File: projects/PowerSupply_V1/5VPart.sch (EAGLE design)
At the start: 26 parts, among them IC1 LM2596T, IC2 LM2596T, X1 IN, X2 OUT

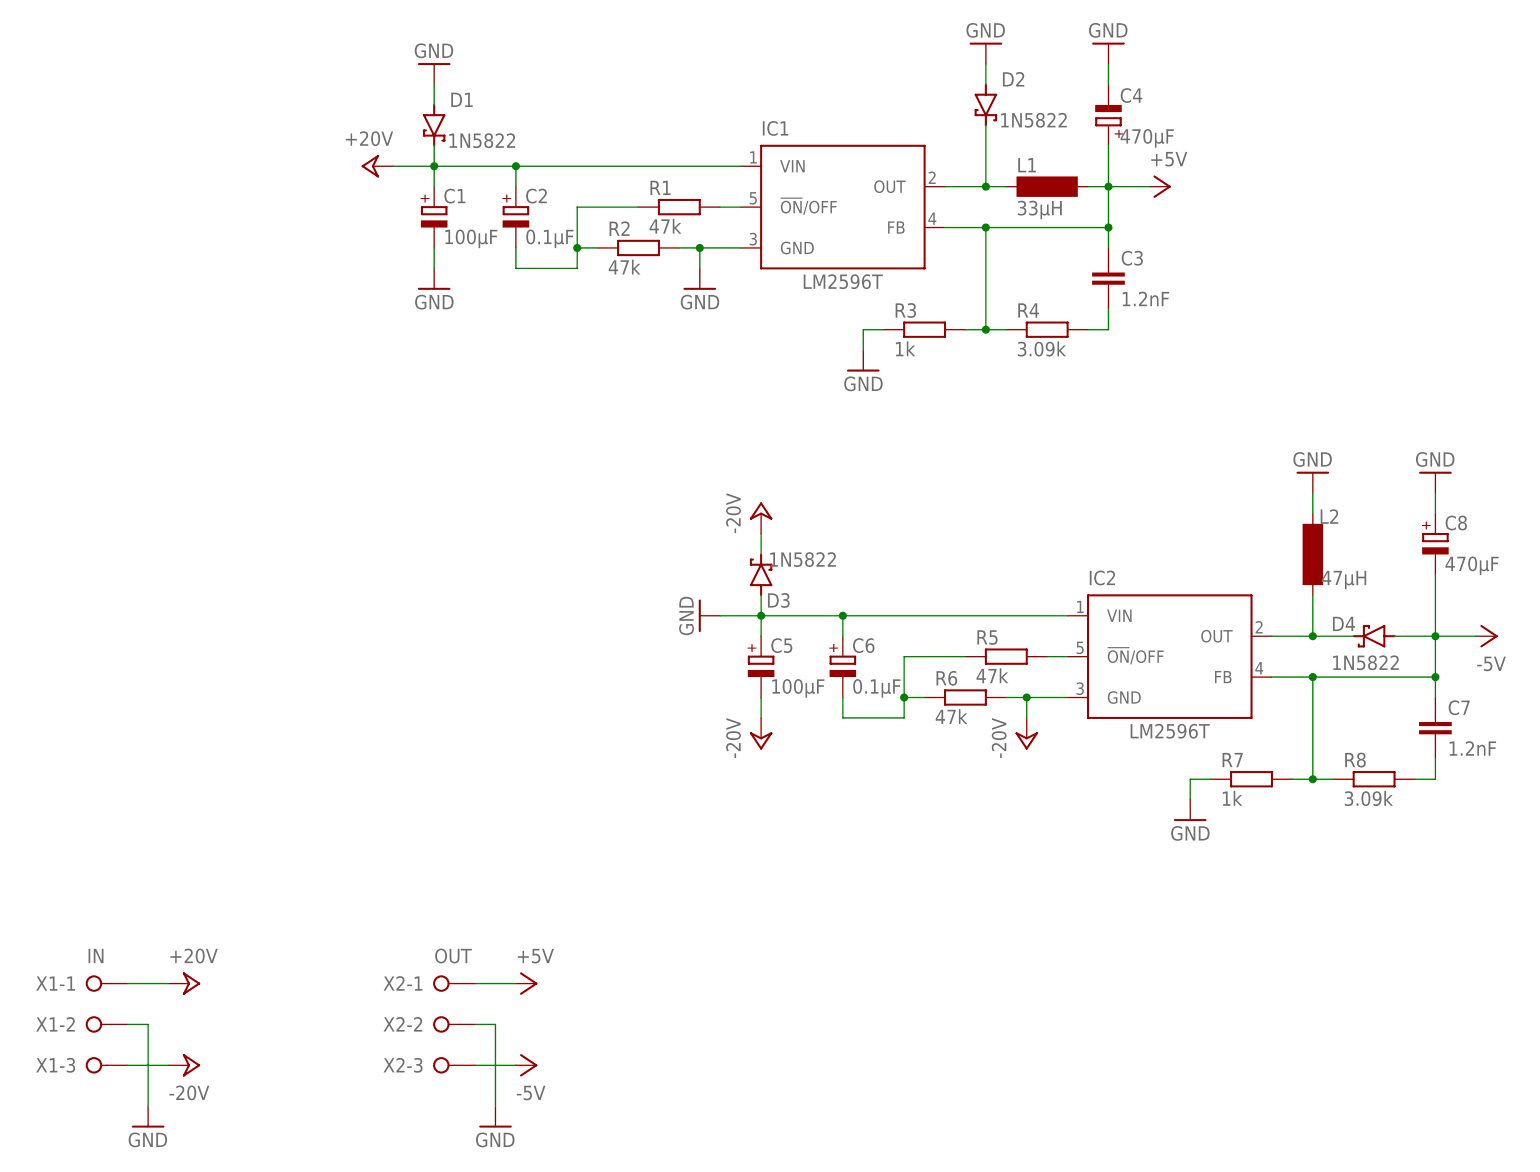
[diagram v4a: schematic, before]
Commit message: refactor(all): schematics and routing changed
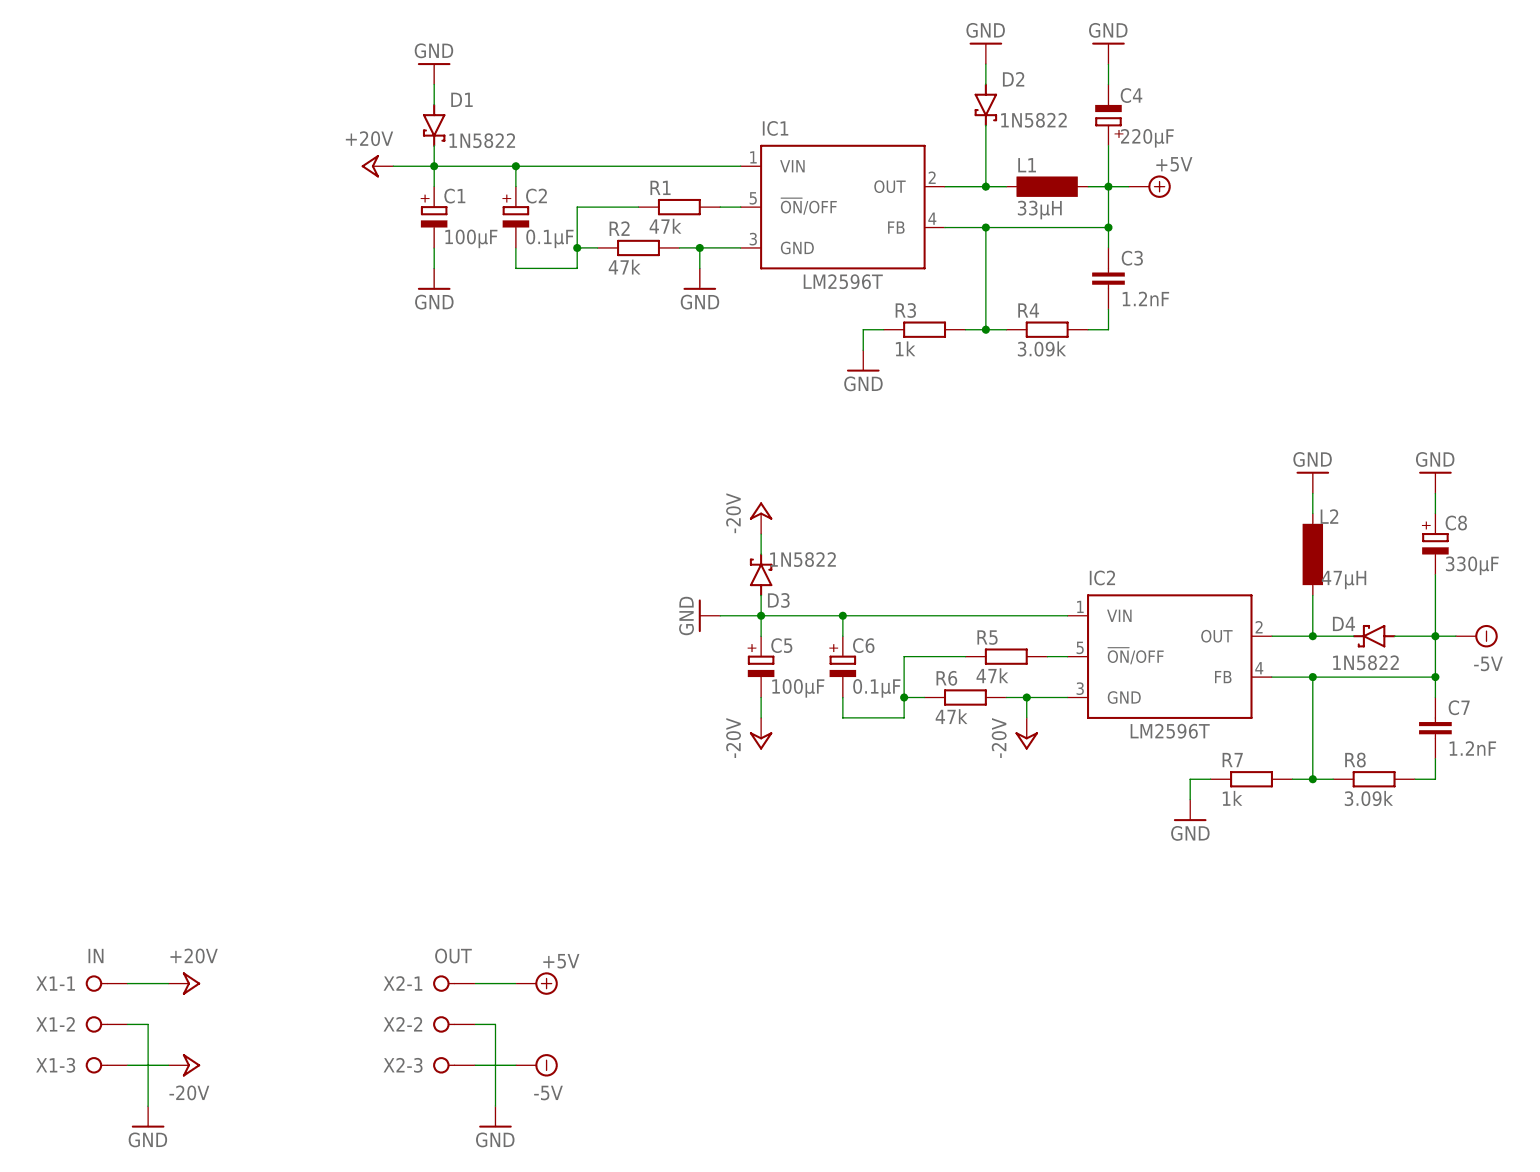
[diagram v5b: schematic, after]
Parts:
- C4: value 470µF -> 220µF
- C8: value 470µF -> 330µF
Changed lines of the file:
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@@
 <part name="GND5" library="supply1" library_urn="urn:adsk.eagle:library:371" deviceset="GND" device=""/>
 <part name="L1" library="inductor-neosid" library_urn="urn:adsk.eagle:library:241" deviceset="SD12" device="-680" package3d_urn="urn:adsk.eagle:package:14657/1" value="33µH"/>
-<part name="C4" library="rcl" library_urn="urn:adsk.eagle:library:334" deviceset="CPOL-EU" device="E3.5-8" package3d_urn="urn:adsk.eagle:package:23360/2" value="470µF"/>
+<part name="C4" library="rcl" library_urn="urn:adsk.eagle:library:334" deviceset="CPOL-EU" device="E3.5-8" package3d_urn="urn:adsk.eagle:package:23360/2" value="220µF"/>
 <part name="X2" library="con-wago-508" library_urn="urn:adsk.eagle:library:196" deviceset="W237-03P" device="" package3d_urn="urn:adsk.eagle:package:10737/1" value="OUT"/>
 <part name="GND7" library="supply1" library_urn="urn:adsk.eagle:library:371" deviceset="GND" device=""/>
@@
 <part name="GND9" library="supply1" library_urn="urn:adsk.eagle:library:371" deviceset="GND" device=""/>
 <part name="D4" library="diode" library_urn="urn:adsk.eagle:library:210" deviceset="SCHOTTKY-DIODE" device="C4111-15" package3d_urn="urn:adsk.eagle:package:43355/2" value="1N5822"/>
-<part name="C8" library="rcl" library_urn="urn:adsk.eagle:library:334" deviceset="CPOL-EU" device="E3.5-8" package3d_urn="urn:adsk.eagle:package:23360/2" value="470µF"/>
+<part name="C8" library="rcl" library_urn="urn:adsk.eagle:library:334" deviceset="CPOL-EU" device="E3.5-8" package3d_urn="urn:adsk.eagle:package:23360/2" value="330µF"/>
 <part name="R7" library="rcl" library_urn="urn:adsk.eagle:library:334" deviceset="R-EU_" device="0207/10" package3d_urn="urn:adsk.eagle:package:23491/2" value="1k"/>
 <part name="R8" library="rcl" library_urn="urn:adsk.eagle:library:334" deviceset="R-EU_" device="0207/10" package3d_urn="urn:adsk.eagle:package:23491/2" value="3.09k"/>
@@
 <part name="R6" library="rcl" library_urn="urn:adsk.eagle:library:334" deviceset="R-EU_" device="0207/10" package3d_urn="urn:adsk.eagle:package:23491/2" value="47k"/>
 <part name="GND8" library="supply1" library_urn="urn:adsk.eagle:library:371" deviceset="GND" device=""/>
-<part name="P+3" library="supply1" library_urn="urn:adsk.eagle:library:371" deviceset="+5V" device=""/>
-<part name="P-6" library="supply1" library_urn="urn:adsk.eagle:library:371" deviceset="-5V" device=""/>
-<part name="P-1" library="supply1" library_urn="urn:adsk.eagle:library:371" deviceset="-5V" device=""/>
-<part name="P+5" library="supply1" library_urn="urn:adsk.eagle:library:371" deviceset="+5V" device=""/>
 <part name="D1" library="diode" library_urn="urn:adsk.eagle:library:210" deviceset="SCHOTTKY-DIODE" device="C4111-15" package3d_urn="urn:adsk.eagle:package:43355/2" value="1N5822"/>
 <part name="GND12" library="supply1" library_urn="urn:adsk.eagle:library:371" deviceset="GND" device=""/>
 <part name="D3" library="diode" library_urn="urn:adsk.eagle:library:210" deviceset="SCHOTTKY-DIODE" device="C4111-15" package3d_urn="urn:adsk.eagle:package:43355/2" value="1N5822"/>
 <part name="P-2" library="supply1" library_urn="urn:adsk.eagle:library:371" deviceset="-24V" device="" value="-20V"/>
+<part name="SUPPLY1" library="supply2" library_urn="urn:adsk.eagle:library:372" deviceset="+5V" device=""/>
+<part name="SUPPLY2" library="supply2" library_urn="urn:adsk.eagle:library:372" deviceset="-5V" device=""/>
+<part name="SUPPLY3" library="supply2" library_urn="urn:adsk.eagle:library:372" deviceset="+5V" device=""/>
+<part name="SUPPLY4" library="supply2" library_urn="urn:adsk.eagle:library:372" deviceset="-5V" device=""/>
 </parts>
 <sheets>
@@
 <attribute name="VALUE" x="91.44" y="71.12" size="1.778" layer="96" rot="MR90"/>
 </instance>
-<instance part="P+3" gate="1" x="73.66" y="27.94" smashed="yes" rot="R270">
-<attribute name="VALUE" x="71.12" y="30.48" size="1.778" layer="96"/>
-</instance>
-<instance part="P-6" gate="1" x="73.66" y="17.78" smashed="yes" rot="R90">
-<attribute name="VALUE" x="71.12" y="15.24" size="1.778" layer="96" rot="MR180"/>
-</instance>
-<instance part="P-1" gate="1" x="193.04" y="71.12" smashed="yes" rot="R90">
-<attribute name="VALUE" x="190.5" y="68.58" size="1.778" layer="96" rot="MR180"/>
-</instance>
-<instance part="P+5" gate="1" x="152.4" y="127" smashed="yes" rot="R270">
-<attribute name="VALUE" x="149.86" y="129.54" size="1.778" layer="96"/>
-</instance>
 <instance part="D1" gate="G$1" x="60.96" y="134.62" smashed="yes" rot="R270">
 <attribute name="NAME" x="62.865" y="136.906" size="1.778" layer="95"/>
@@
 <instance part="P-2" gate="1" x="101.6" y="86.36" smashed="yes" rot="R180">
 <attribute name="VALUE" x="99.06" y="83.82" size="1.778" layer="96" rot="R90"/>
+</instance>
+<instance part="SUPPLY1" gate="+5V" x="73.66" y="27.94" smashed="yes" rot="R270">
+<attribute name="VALUE" x="74.295" y="29.845" size="1.778" layer="96"/>
+</instance>
+<instance part="SUPPLY2" gate="-5V" x="73.66" y="17.78" smashed="yes" rot="MR270">
+<attribute name="VALUE" x="73.279" y="15.24" size="1.778" layer="96" rot="MR180"/>
+</instance>
+<instance part="SUPPLY3" gate="+5V" x="149.86" y="127" smashed="yes" rot="R270">
+<attribute name="VALUE" x="150.495" y="128.905" size="1.778" layer="96"/>
+</instance>
+<instance part="SUPPLY4" gate="-5V" x="190.5" y="71.12" smashed="yes" rot="MR270">
+<attribute name="VALUE" x="190.119" y="68.58" size="1.778" layer="96" rot="MR180"/>
 </instance>
 </instances>
@@
 <pinref part="X2" gate="-1" pin="KL"/>
 <wire x1="66.04" y1="27.94" x2="71.12" y2="27.94" width="0.1524" layer="91"/>
-<pinref part="P+3" gate="1" pin="+5V"/>
+<pinref part="SUPPLY1" gate="+5V" pin="+5V"/>
 </segment>
 <segment>
@@
 <wire x1="142.24" y1="127" x2="144.78" y2="127" width="0.1524" layer="91"/>
 <wire x1="144.78" y1="127" x2="144.78" y2="121.92" width="0.1524" layer="91"/>
-<wire x1="144.78" y1="127" x2="149.86" y2="127" width="0.1524" layer="91"/>
+<wire x1="144.78" y1="127" x2="147.32" y2="127" width="0.1524" layer="91"/>
 <junction x="144.78" y="127"/>
 <pinref part="C4" gate="G$1" pin="+"/>
 <wire x1="144.78" y1="132.08" x2="144.78" y2="127" width="0.1524" layer="91"/>
-<pinref part="P+5" gate="1" pin="+5V"/>
+<pinref part="SUPPLY3" gate="+5V" pin="+5V"/>
 </segment>
 </net>
 <net name="-5V" class="0">
 <segment>
-<wire x1="185.42" y1="71.12" x2="190.5" y2="71.12" width="0.1524" layer="91"/>
+<pinref part="X2" gate="-3" pin="KL"/>
+<wire x1="66.04" y1="17.78" x2="71.12" y2="17.78" width="0.1524" layer="91"/>
+<pinref part="SUPPLY2" gate="-5V" pin="-5V"/>
+</segment>
+<segment>
+<wire x1="185.42" y1="71.12" x2="187.96" y2="71.12" width="0.1524" layer="91"/>
 <pinref part="C8" gate="G$1" pin="-"/>
 <wire x1="185.42" y1="78.74" x2="185.42" y2="71.12" width="0.1524" layer="91"/>
@@
 <pinref part="D4" gate="G$1" pin="A"/>
 <wire x1="180.34" y1="71.12" x2="185.42" y2="71.12" width="0.1524" layer="91"/>
-<pinref part="P-1" gate="1" pin="-5V"/>
-</segment>
-<segment>
-<pinref part="X2" gate="-3" pin="KL"/>
-<pinref part="P-6" gate="1" pin="-5V"/>
-<wire x1="66.04" y1="17.78" x2="71.12" y2="17.78" width="0.1524" layer="91"/>
-</segment>
-</net>
+<pinref part="SUPPLY4" gate="-5V" pin="-5V"/>
+</segment>
+</net>

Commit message: feat: 5VPart refactored
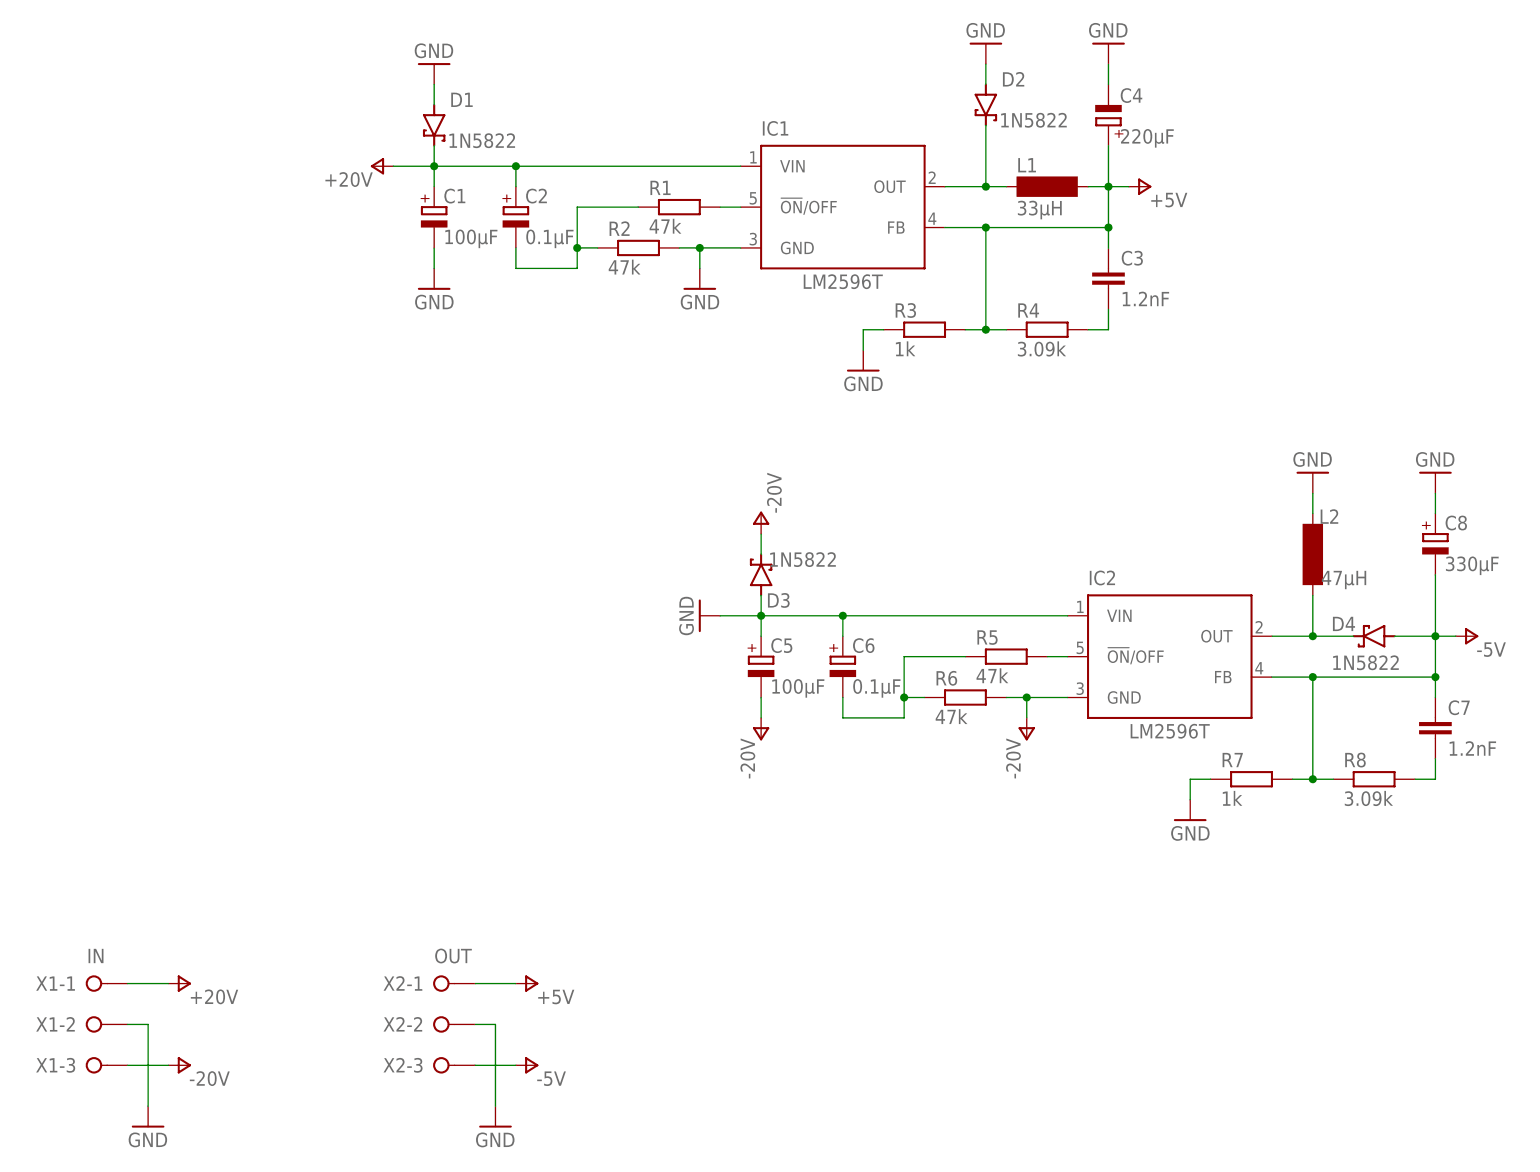
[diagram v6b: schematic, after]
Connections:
- net +24V renamed +20V
- net -24V renamed -20V
